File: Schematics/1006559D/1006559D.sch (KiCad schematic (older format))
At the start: 9 parts, among them J1 ConnectorBlockI, X1 OvalBody2, X2 NorBody, X3 ArrowTwiddle, X4 ArrowTwiddle

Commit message: Placed some components and wires on CAD for drawing 1006559D.
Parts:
- added unit 15 of J1
- added unit 111 of J1
- added unit 17 of J1
- added unit 51 of J1
- added unit 19 of J1
- added unit 39 of J1
- added unit 37 of J1
- added unit 33 of J1
- added unit 99 of J1
- added unit 105 of J1
- added unit 97 of J1
- added unit 7 of J1
- added unit 113 of J1
- added unit 107 of J1
- added unit 49 of J1
- added unit 41 of J1
- added unit 9 of J1
- added unit 21 of J1
- added unit 5 of J1
- added unit 77 of J1
- added unit 115 of J1
- added unit 117 of J1
- added unit 137 of J1
- added unit 53 of J1
- added unit 135 of J1
- added unit 55 of J1
- added unit 35 of J1
- added unit 79 of J1
- added unit 67 of J1
- added unit 69 of J1
- added unit 45 of J1
- added unit 125 of J1
- added unit 127 of J1
- added unit 1 of J1
- added unit 103 of J1
- added unit 101 of J1
- added unit 81 of J1
- added unit 87 of J1
- added unit 109 of J1
- added unit 89 of J1
- added unit 91 of J1
- added unit 102 of J1
- added unit 133 of J1
- added unit 130 of J1
- added unit 32 of J1
- added unit 31 of J1
- added unit 98 of J1
- added unit 12 of J1
- added unit 129 of J1
- added unit 121 of J1
- added unit 123 of J1
- added unit 124 of J1
- added unit 20 of J1
- added unit 22 of J1
- added unit 70 of J1
- added unit 114 of J1
- added unit 116 of J1
- added unit 74 of J1
- added unit 118 of J1
- added unit 50 of J1
- added unit 52 of J1
- added unit 54 of J1
- added unit 78 of J1
- added unit 38 of J1
- added unit 36 of J1
- added unit 34 of J1
- added unit 106 of J1
- added unit 62 of J1
- added unit 64 of J1
- added unit 68 of J1
- added unit 108 of J1
- added unit 29 of J1
- added unit 3 of J1
- added unit 84 of J1
- added U1, U101, U15, U18, U61, U7: D3NOR-+3VDC-0VDC-block1-_3_-___, symbol D3NOR-+3VDC-0VDC-block1:D3NOR-+3VDC-0VDC-block1-_3_-___
- added U10, U17: D3NOR-+3VDC-0VDC-block1-31_-___, symbol D3NOR-+3VDC-0VDC-block1:D3NOR-+3VDC-0VDC-block1-31_-___
- added U100, U104, U32, U43, U44, U56, U60, U64, U92: D3NOR-NC-0VDC-expander-block1-3_5-___, symbol D3NOR-NC-0VDC-expander-block1:D3NOR-NC-0VDC-expander-block1-3_5-___
- added U105, U49, U69, U85, U89, U97: D3NOR-+3VDC-0VDC-block1-_1_-___, symbol D3NOR-+3VDC-0VDC-block1:D3NOR-+3VDC-0VDC-block1-_1_-___
- added U106, U26, U42, U46, U70, U73, U81: D3NOR-+3VDC-0VDC-block1-1_3-___, symbol D3NOR-+3VDC-0VDC-block1:D3NOR-+3VDC-0VDC-block1-1_3-___
- added U107, U91, U99: D3NOR-NC-0VDC-expander-block1-_5_-___, symbol D3NOR-NC-0VDC-expander-block1:D3NOR-NC-0VDC-expander-block1-_5_-___
- added U115, U37, U45, U57, U65, U75, U83, U95: D3NOR-NC-0VDC-expander-block1-_3_-___, symbol D3NOR-NC-0VDC-expander-block1:D3NOR-NC-0VDC-expander-block1-_3_-___
- added U12, U28, U35, U72, U91: D3NOR-+3VDC-0VDC-block1-3_5-___, symbol D3NOR-+3VDC-0VDC-block1:D3NOR-+3VDC-0VDC-block1-3_5-___
- added U13, U33, U5: D3NOR-+3VDC-0VDC-block1-1_5-___, symbol D3NOR-+3VDC-0VDC-block1:D3NOR-+3VDC-0VDC-block1-1_5-___
- added U18, U20, U25, U31, U93: D3NOR-+3VDC-0VDC-block1-_5_-___, symbol D3NOR-+3VDC-0VDC-block1:D3NOR-+3VDC-0VDC-block1-_5_-___
- added U27: D3NOR-+3VDC-0VDC-block1-135-___, symbol D3NOR-+3VDC-0VDC-block1:D3NOR-+3VDC-0VDC-block1-135-___
- added U3, U48: D3NOR-+3VDC-0VDC-block1-315-___, symbol D3NOR-+3VDC-0VDC-block1:D3NOR-+3VDC-0VDC-block1-315-___
- added U39, U47, U59, U67: D3NOR-+3VDC-0VDC-block1-153-___, symbol D3NOR-+3VDC-0VDC-block1:D3NOR-+3VDC-0VDC-block1-153-___
- added U77: D3NOR-NC-0VDC-expander-block1-1_3-___, symbol D3NOR-NC-0VDC-expander-block1:D3NOR-NC-0VDC-expander-block1-1_3-___
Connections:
- wire segments 36 -> 272
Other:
- note added: "1006559"
- note added: "2M5\n88090"
- note added: "A REVISED PER TDRR 03608"
- note added: "B REVISED PER TDRR 04148"
- note added: "C REVISED PER TDRR 06015"
- note added: "D REVISED PER TDRR 06234"
- note added: "LOGIC FLOW "V""
- note added: "LOGIC MODULE NO. A29"
- note added: "Notes from the Virtual AGC Project:\n1. This CAD drawing was transcribed from the original Apollo Program drawing 1006559D. — RSB 2019\n2. The original drawing did not show reference designators or pin numbers for the NOR gates, so this \n CAD drawing does not show them either. That information has been taken instead from the signal \n wiring diagram, drawing 1006139A. Though not visible, referen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"
- note added: "REFERENCE"
- note removed: "//"
- note removed: "1006544"
- note removed: "2M5\n35090"
- note removed: "A REVISED PER TDRR 03683"
- note removed: "B REVISED PER TDRR 04174"
- note removed: "LOGIC FLOW D"
- note removed: "LOGIC MODULE NO. A27"
- note removed: "Notes from the Virtual AGC Project:\n1. This CAD drawing was transcribed from the original Apollo Program drawing \n 1006559D. — RSB 2019\n2. The original drawing did not show reference designators or pin numbers for \n the NOR gates, so this CAD drawing does not show them either. That \n information has been taken instead from the signal wiring diagram, drawing\n 1006139A. Though not visible, re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"
- note removed: "___"
- note removed: "____________"
- note removed: "{"
- moved on the sheet: C1, C2, C3, C4

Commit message: Finished placing components and routing wires on drawing 1006559D, but still need to add in some net labels and do some proofing before the CAD transcription will be complete.
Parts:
- added unit 73 of J1
- added unit 76 of J1
- added unit 75 of J1
- added unit 46 of J1
- added unit 44 of J1
- added unit 88 of J1
- added unit 59 of J1
- added unit 58 of J1
- added unit 112 of J1
- added unit 61 of J1
- added unit 57 of J1
- added unit 100 of J1
- added unit 28 of J1
- added unit 26 of J1
- added unit 27 of J1
- added unit 138 of J1
- added unit 139 of J1
- added unit 134 of J1
- added unit 132 of J1
- added unit 131 of J1
- added unit 25 of J1
- added unit 128 of J1
- added unit 122 of J1
- added unit 126 of J1
- added unit 2 of J1
- added unit 83 of J1
- added unit 85 of J1
- added unit 110 of J1
- added unit 14 of J1
- added unit 16 of J1
- added unit 11 of J1
- added unit 13 of J1
- added unit 63 of J1
- added unit 65 of J1
- added unit 66 of J1
- added unit 142 of J1
- added unit 141 of J1
- added unit 140 of J1
- added U102, U54, U62, U94: D3NOR-NC-0VDC-expander-block1-_1_-___, symbol D3NOR-NC-0VDC-expander-block1:D3NOR-NC-0VDC-expander-block1-_1_-___
- added U103: D3NOR-+3VDC-0VDC-block1-_5_-___, symbol D3NOR-+3VDC-0VDC-block1:D3NOR-+3VDC-0VDC-block1-_5_-___
- added U108, U11, U112, U23, U55, U63, U71: D3NOR-NC-0VDC-expander-block1-3_5-___, symbol D3NOR-NC-0VDC-expander-block1:D3NOR-NC-0VDC-expander-block1-3_5-___
- added U109, U110, U117, U90: D3NOR-+3VDC-0VDC-block1-31_-___, symbol D3NOR-+3VDC-0VDC-block1:D3NOR-+3VDC-0VDC-block1-31_-___
- added U111, U119: D3NOR-+3VDC-0VDC-block1-35_-___, symbol D3NOR-+3VDC-0VDC-block1:D3NOR-+3VDC-0VDC-block1-35_-___
- added U113: D3NOR-+3VDC-0VDC-block1-1_5-___, symbol D3NOR-+3VDC-0VDC-block1:D3NOR-+3VDC-0VDC-block1-1_5-___
- added U114, U118, U34, U50, U6, U66, U78, U86: D3NOR-+3VDC-0VDC-block1-1_3-___, symbol D3NOR-+3VDC-0VDC-block1:D3NOR-+3VDC-0VDC-block1-1_3-___
- added U116: D3NOR-+3VDC-0VDC-block1-153-___, symbol D3NOR-+3VDC-0VDC-block1:D3NOR-+3VDC-0VDC-block1-153-___
- added U120, U51, U84: D3NOR-+3VDC-0VDC-block1-3_5-___, symbol D3NOR-+3VDC-0VDC-block1:D3NOR-+3VDC-0VDC-block1-3_5-___
- added U14: D3NOR-+3VDC-0VDC-block1-_3_-___, symbol D3NOR-+3VDC-0VDC-block1:D3NOR-+3VDC-0VDC-block1-_3_-___
- added U16: D3NOR-NC-0VDC-expander-block1-153-___, symbol D3NOR-NC-0VDC-expander-block1:D3NOR-NC-0VDC-expander-block1-153-___
- added U2, U22, U74, U82: D3NOR-NC-0VDC-expander-block1-_3_-___, symbol D3NOR-NC-0VDC-expander-block1:D3NOR-NC-0VDC-expander-block1-_3_-___
- added U24: D3NOR-+3VDC-0VDC-block1-51_-___, symbol D3NOR-+3VDC-0VDC-block1:D3NOR-+3VDC-0VDC-block1-51_-___
- added U30, U38, U4, U58, U76, U98: D3NOR-+3VDC-0VDC-block1-13_-___, symbol D3NOR-+3VDC-0VDC-block1:D3NOR-+3VDC-0VDC-block1-13_-___
- added U36, U40, U52, U68, U8, U80, U88: D3NOR-+3VDC-0VDC-block1-315-___, symbol D3NOR-+3VDC-0VDC-block1:D3NOR-+3VDC-0VDC-block1-315-___
- added U96: D3NOR-NC-0VDC-expander-block1-135-___, symbol D3NOR-NC-0VDC-expander-block1:D3NOR-NC-0VDC-expander-block1-135-___
- added X10, X11, X12, X13, X14, X15, X16, X5, X6, X7, X8, X9: Node2, symbol AGC_DSKY:Node2
- added \1: ConnectorBlockI, symbol AGC_DSKY:ConnectorBlockI
- renumbered U18 to U19, U91 to U87
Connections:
- wire segments 272 -> 529

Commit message: Complete CAD transcription and proofing of drawing 1006559D (Block I AGC module A29 electrical schematic).
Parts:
- U33: agc4 1E5 -> 1G5
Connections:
- net NRPTAL: now reaches U16.1, X6.1
- net NRPTAL: now also U24.7, U36.1, X16.1
- net RPTAL: now reaches U16.3, X9.1
- net RPTAL: now also U4.7, U8.1, X13.1
- net NCTRAL: now reaches U116.5, U120.7, X15.1
- net NCTRAL: now also U96.5, X8.1
- net CTRAL: now reaches U88.1, U98.7, X14.1
- net CTRAL: now also U96.3, X5.1
- net NTCAL: now reaches U68.1, U76.7, X12.1
- net NTCAL: now also U96.1, X10.1
- net TCAL: now reaches U38.7, U52.1, X11.1
- net TCAL: now also U40.1, X7.1

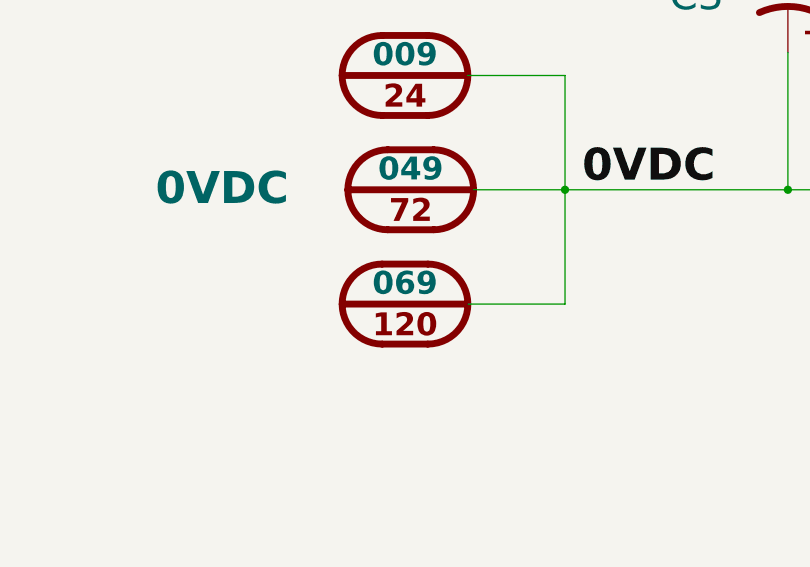
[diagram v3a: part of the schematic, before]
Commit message: Apparently, in the first Block I AGC drawing I transcribed to CAD, I misread the AGC4 connector pin name associated with AGC5 connector pin 120 as "69" when it was really "89".  This error had propagated to all of the Block I drawings except the most recent (1006550F) and the transcriptions I had made from ND-1021041 rather than from drawings.
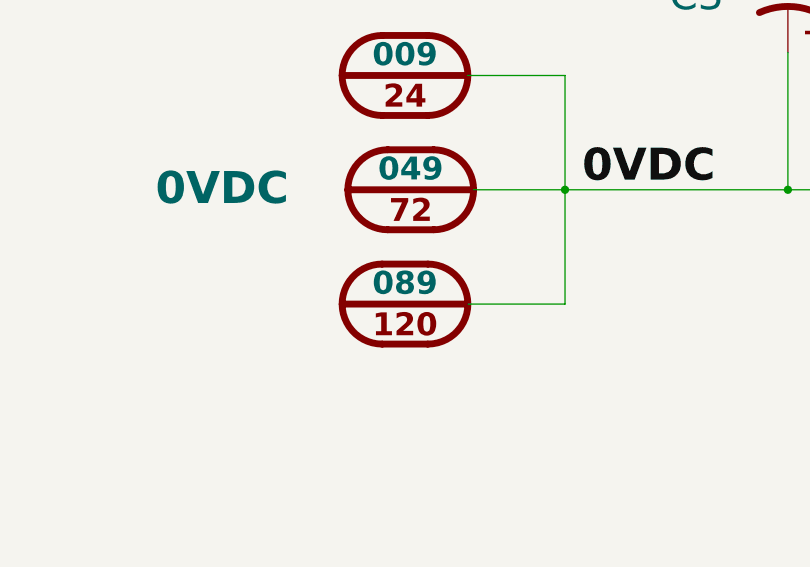
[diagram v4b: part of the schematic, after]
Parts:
- J1: agc4 069 -> 089
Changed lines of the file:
@@
 F 2 "" H 23800 32825 140 0001 C CNN
 F 3 "" H 23800 32825 140 0001 C CNN
-F 4 "069" H 23800 32500 100 0000 C TNB "agc4"
+F 4 "089" H 23800 32500 100 0000 C TNB "agc4"
 F 5 "0VDC" H 23800 32575 140 0001 C BNB "Caption"
 	120  23800 32350
